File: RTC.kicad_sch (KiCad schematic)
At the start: 14 parts, among them J14 Molex 470531000, U10 EMC2301-1-ACZL-TR, U11 74LVC1G07SE-7, U9 PCF85063AT/AAZ, Y2 X32K768S301

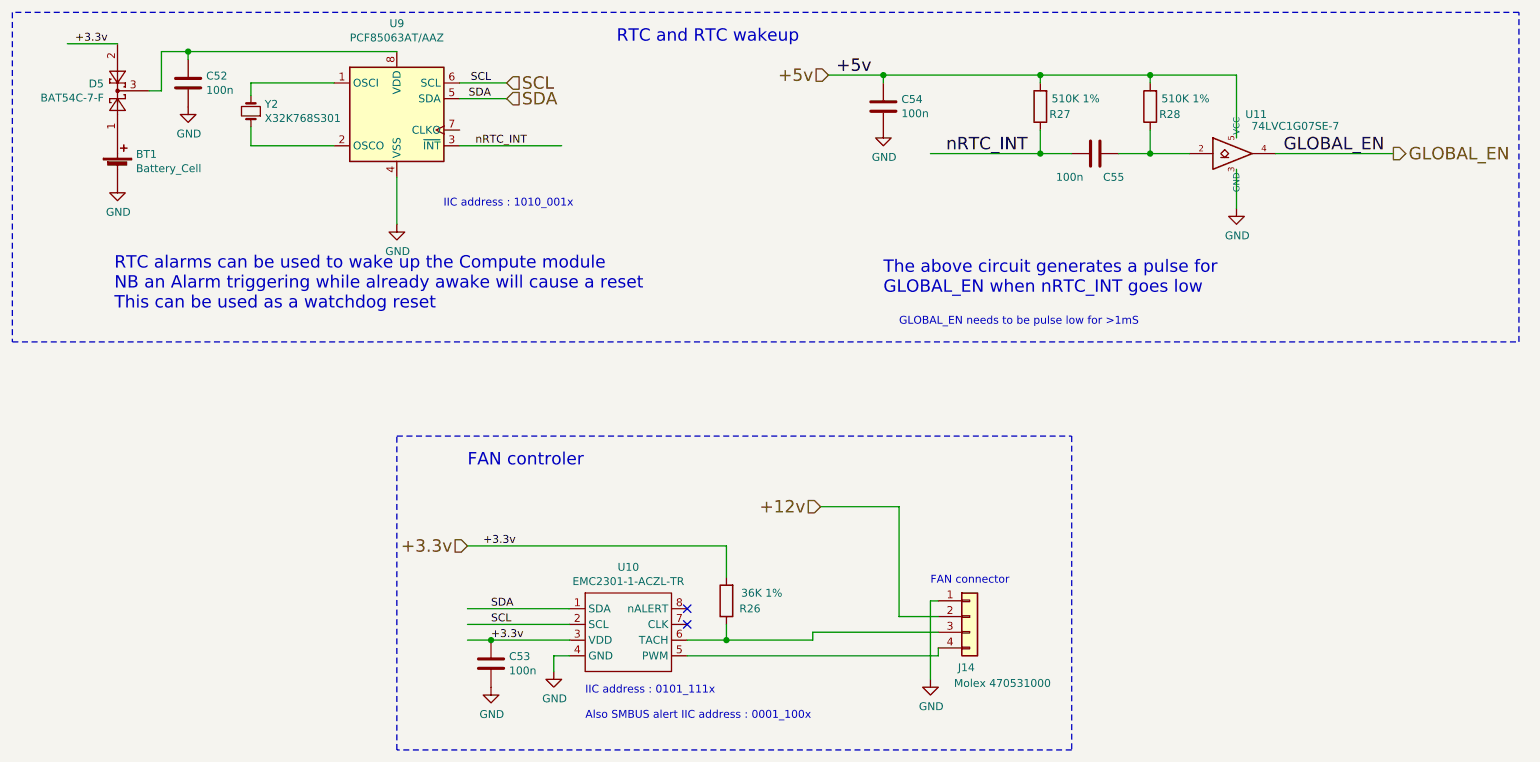
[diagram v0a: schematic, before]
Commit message: Initial layout and all parts added. Some pins still not connected to power
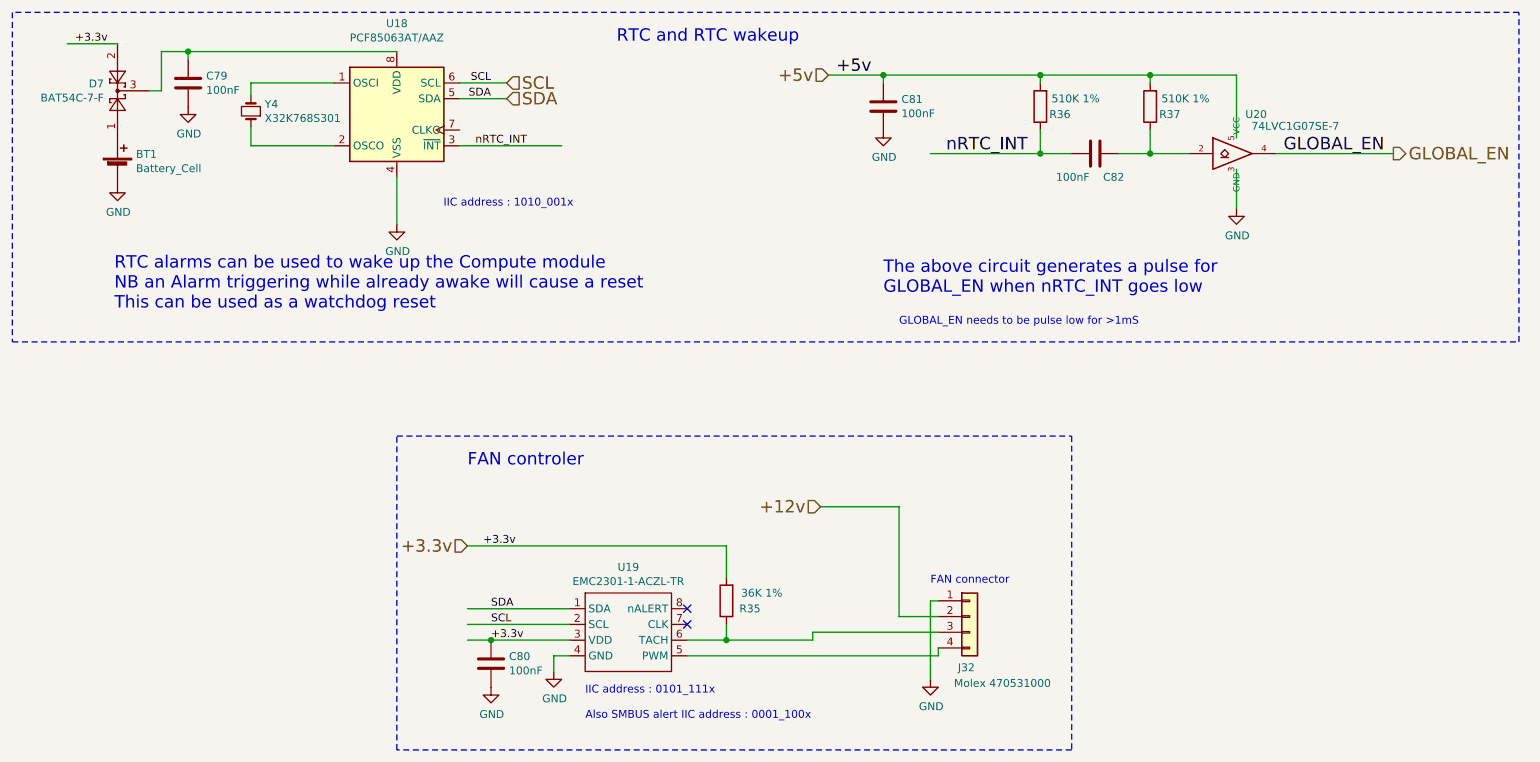
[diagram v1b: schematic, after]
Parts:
- C79: renamed from C52; value 100n -> 100nF
- C80: renamed from C53; value 100n -> 100nF
- C81: renamed from C54; value 100n -> 100nF
- C82: renamed from C55; value 100n -> 100nF
- renumbered D5 to D7, J14 to J32, R26 to R35, R27 to R36, R28 to R37, U9 to U18, U10 to U19, U11 to U20, Y2 to Y4
